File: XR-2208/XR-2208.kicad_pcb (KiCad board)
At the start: 2 copper layers, 83.8 x 40.6 mm, 18 parts, among them IC1 XR-2208, J1 V_x, J2 V_y, J3 V_z

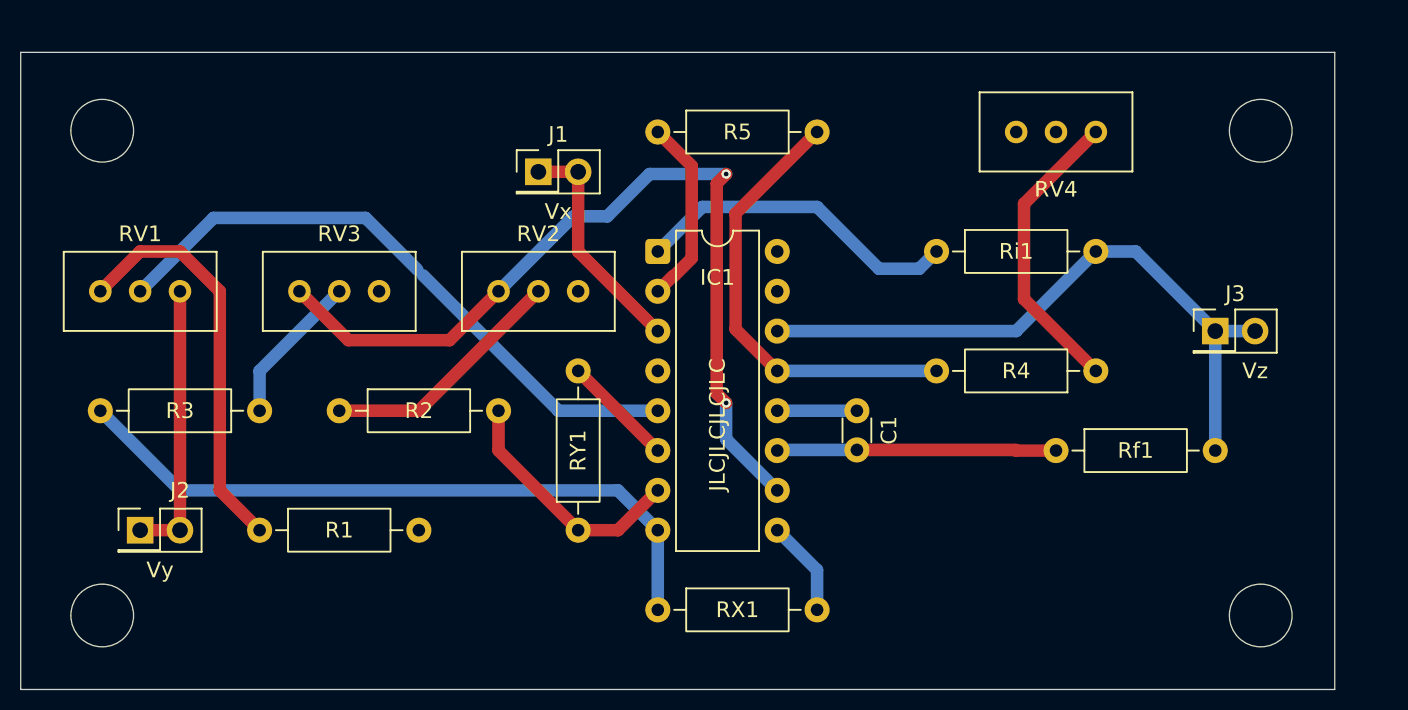
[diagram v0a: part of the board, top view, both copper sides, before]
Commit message: move to back side, 4 vias
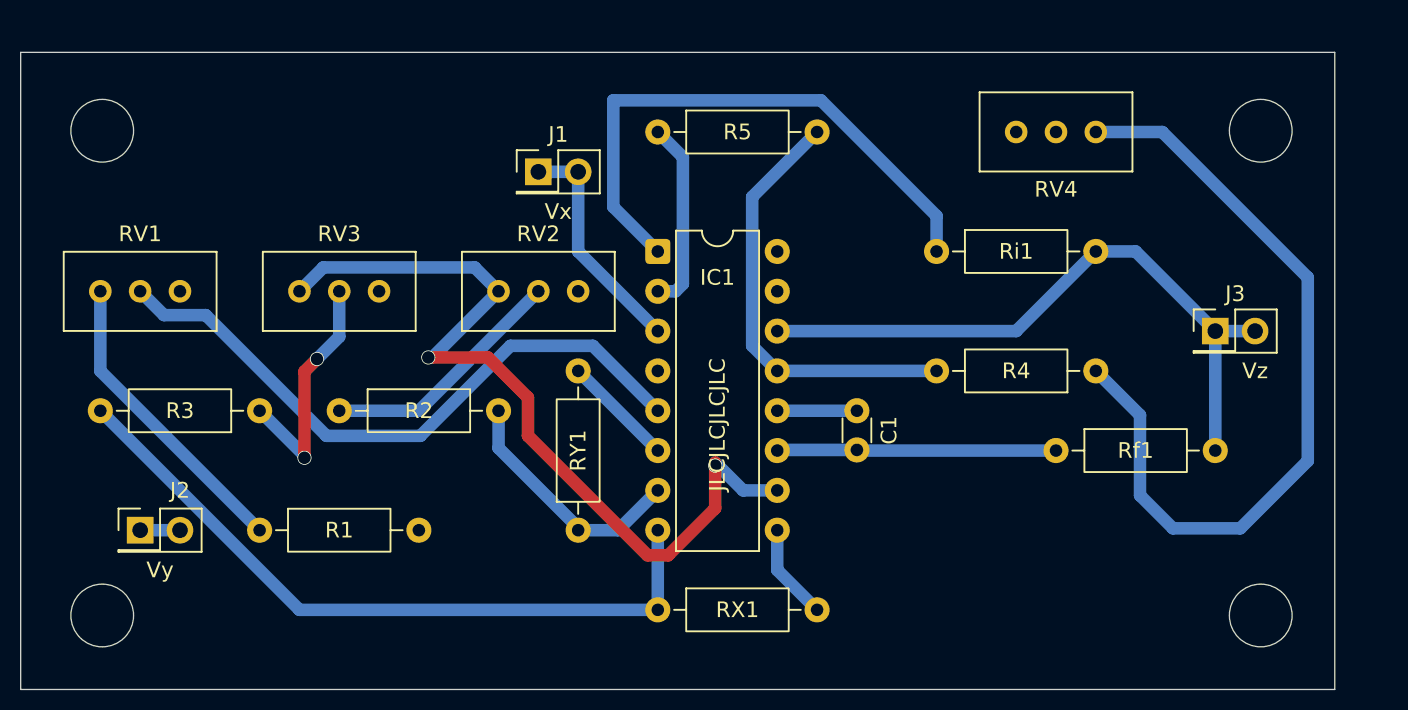
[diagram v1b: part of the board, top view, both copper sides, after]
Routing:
- net Net-(R4-Pad1): track 19.0 -> 51.5 mm
- net Net-(IC1-MULT@1): track 21.0 -> 36.8 mm
- net Net-(J2-Pin_1): track 17.8 -> 2.54 mm
- net Net-(R1-Pad1): track 26.0 -> 19.4 mm
- net Net-(R3-Pad1): track 9.72 -> 15.7 mm, vias 0 -> 2
- net Net-(IC1-X_GAIN@1): track 43.8 -> 45.9 mm
- net Net-(IC1-Y_IN): track 39.5 -> 40.9 mm
- net VEE: track 54.9 -> 54.0 mm
- net Net-(IC1-OP+): track 28.7 -> 27.8 mm

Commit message: fix
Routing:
- net GND: track 0.00 -> 35.9 mm, vias 0 -> 2
- net VEE: track 54.0 -> 55.8 mm
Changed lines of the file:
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@@
+	)
+	(segment
+		(start 134.9 102.1)
+		(end 134.9 107.822626)
+		(width 0.8)
+		(layer "F.Cu")
+		(net 3)
+	)
+	(segment
+		(start 118.822 112.022)
+		(end 117.65 110.85)
+		(width 0.8)
+		(layer "F.Cu")
+		(net 3)
+	)
+	(segment
+		(start 134.9 107.822626)
+		(end 130.700626 112.022)
+		(width 0.8)
+		(layer "F.Cu")
+		(net 3)
+	)
+	(segment
+		(start 117.65 110.85)
+		(end 117.6 110.8)
+		(width 0.8)
+		(layer "F.Cu")
+		(net 3)
+	)
+	(segment
+		(start 130.700626 112.022)
+		(end 118.822 112.022)
+		(width 0.8)
+		(layer "F.Cu")
+		(net 3)
+	)
+	(via
+		(at 134.9 102.1)
+		(size 0.9)
+		(drill 0.8)
+		(layers "F.Cu" "B.Cu")
+		(net 3)
+	)
+	(via
+		(at 117.65 110.85)
+		(size 0.9)
+		(drill 0.8)
+		(layers "F.Cu" "B.Cu")
+		(net 3)
+	)
+	(segment
+		(start 115.93 110.85)
+		(end 114.3 109.22)
+		(width 0.8)
+		(layer "B.Cu")
+		(net 3)
+	)
+	(segment
+		(start 117.65 110.85)
+		(end 115.93 110.85)
+		(width 0.8)
+		(layer "B.Cu")
+		(net 3)
+	)
+	(segment
+		(start 131.86 99.06)
+		(end 134.9 102.1)
+		(width 0.8)
+		(layer "B.Cu")
+		(net 3)
+	)
+	(segment
+		(start 129.54 99.06)
+		(end 131.86 99.06)
+		(width 0.8)
+		(layer "B.Cu")
+		(net 3)
 	)
 	(segment
@@
 	)
 	(segment
+		(start 132.3 104)
+		(end 132.3 108.724156)
+		(width 0.8)
+		(layer "F.Cu")
+		(net 12)
+	)
+	(segment
+		(start 132.3 108.724156)
+		(end 130.203156 110.821)
+		(width 0.8)
+		(layer "F.Cu")
+		(net 12)
+	)
+	(segment
 		(start 121.256844 100.756844)
 		(end 118.7 98.2)
@@
 	)
 	(segment
-		(start 133.2 104.9)
-		(end 133.2 105.1)
-		(width 0.8)
-		(layer "F.Cu")
-		(net 12)
-	)
-	(segment
-		(start 133.2 105.1)
-		(end 133.2 107.824156)
-		(width 0.8)
-		(layer "F.Cu")
-		(net 12)
-	)
-	(segment
 		(start 118.7 98.2)
 		(end 114.9 98.2)
@@
 	)
 	(segment
-		(start 133.2 107.824156)
-		(end 130.203156 110.821)
-		(width 0.8)
-		(layer "F.Cu")
-		(net 12)
-	)
-	(segment
 		(start 121.256844 103.201)
 		(end 121.256844 100.756844)
@@
 		(width 0.8)
 		(layer "F.Cu")
+		(net 12)
+	)
+	(via
+		(at 132.3 104)
+		(size 0.9)
+		(drill 0.8)
+		(layers "F.Cu" "B.Cu")
 		(net 12)
 	)
@@
 		(net 12)
 	)
-	(via
-		(at 133.2 105.1)
-		(size 0.9)
-		(drill 0.8)
-		(layers "F.Cu" "B.Cu")
-		(net 12)
-	)
 	(segment
 		(start 137.16 106.68)
@@
 	)
 	(segment
+		(start 134.98 106.68)
+		(end 132.3 104)
+		(width 0.8)
+		(layer "B.Cu")
+		(net 12)
+	)
+	(segment
 		(start 114.9 98.2)
 		(end 115.16 98.2)
@@
 		(width 0.8)
 		(layer "B.Cu")
-		(net 12)
-	)
-	(segment
-		(start 134.98 106.68)
-		(end 133.2 104.9)
-		(width 0.8)
-		(layer "B.Cu")

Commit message: fix board
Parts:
- added J4: VCC, Connector_PinHeader_2.54mm:PinHeader_2x01_P2.54mm_Vertical, F.Cu at (159.2, 116.5)
- added J5: GND, Connector_PinHeader_2.54mm:PinHeader_2x01_P2.54mm_Vertical, F.Cu at (152.2, 116.5)
- added J6: VEE, Connector_PinHeader_2.54mm:PinHeader_2x01_P2.54mm_Vertical, F.Cu at (144.5, 116.5)
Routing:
- net VCC: track 0.00 -> 194.5 mm
- net GND: track 35.9 -> 75.1 mm, vias 2 -> 3
- net Net-(J2-Pin_1): track 2.54 -> 27.8 mm
- net VEE: track 55.8 -> 71.2 mm
